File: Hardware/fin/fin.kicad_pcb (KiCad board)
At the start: 2 copper layers, 165.1 x 69.8 mm, 44 parts, among them J1 Conn_01x07, J2 Conn_01x04_Pin, J3 Conn_01x04_Pin, J4 Conn_ARM_SWD_TagConnect_TC203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, J5 Conn_01x04_Pin, U1 ADS131M03QPWRQ1, U2 ADXL380-1BCCZ-RL7, U3 W25N512GVEIG, U4 TMP235A4DBZR, U5 STM32L412K8Ux, U6 ADXL380-1BCCZ-RL7, X1 ECS-327TXO-33-TR

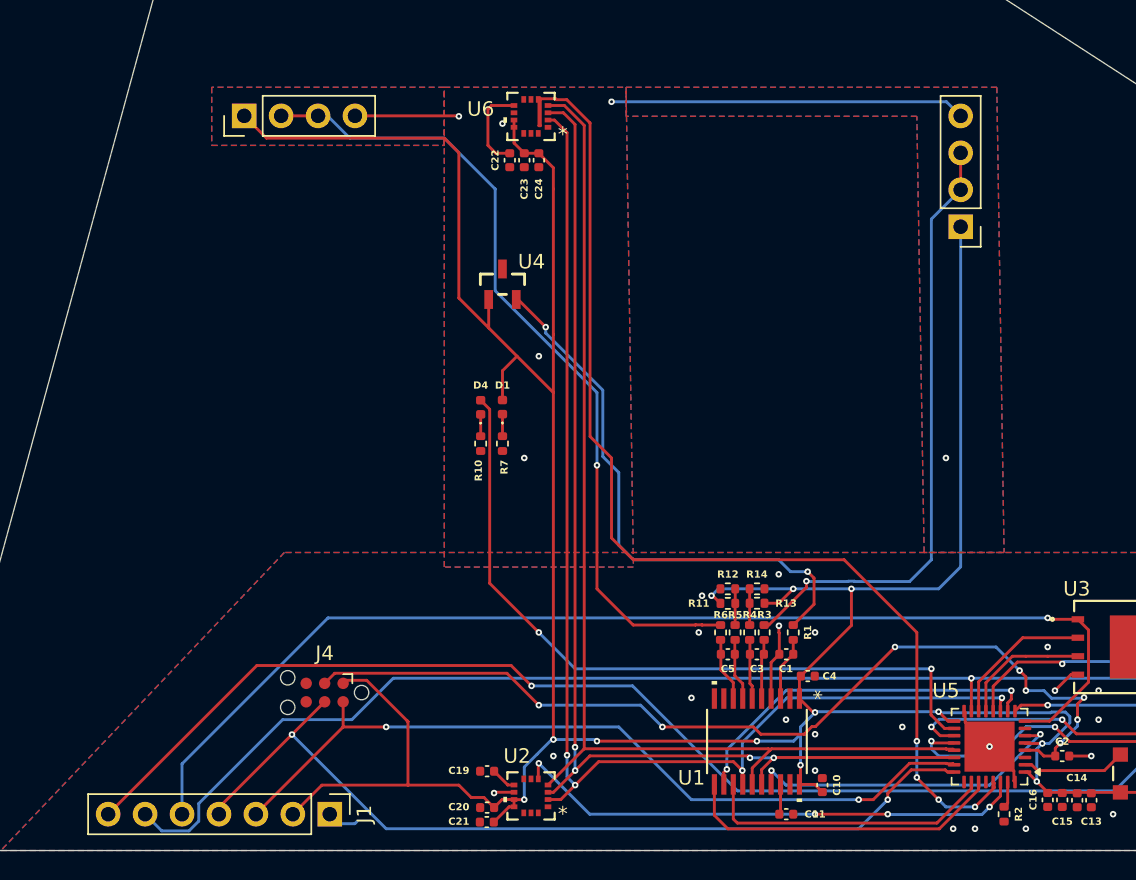
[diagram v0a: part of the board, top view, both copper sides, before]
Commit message: add panel drawing and change connector footprint to use slots
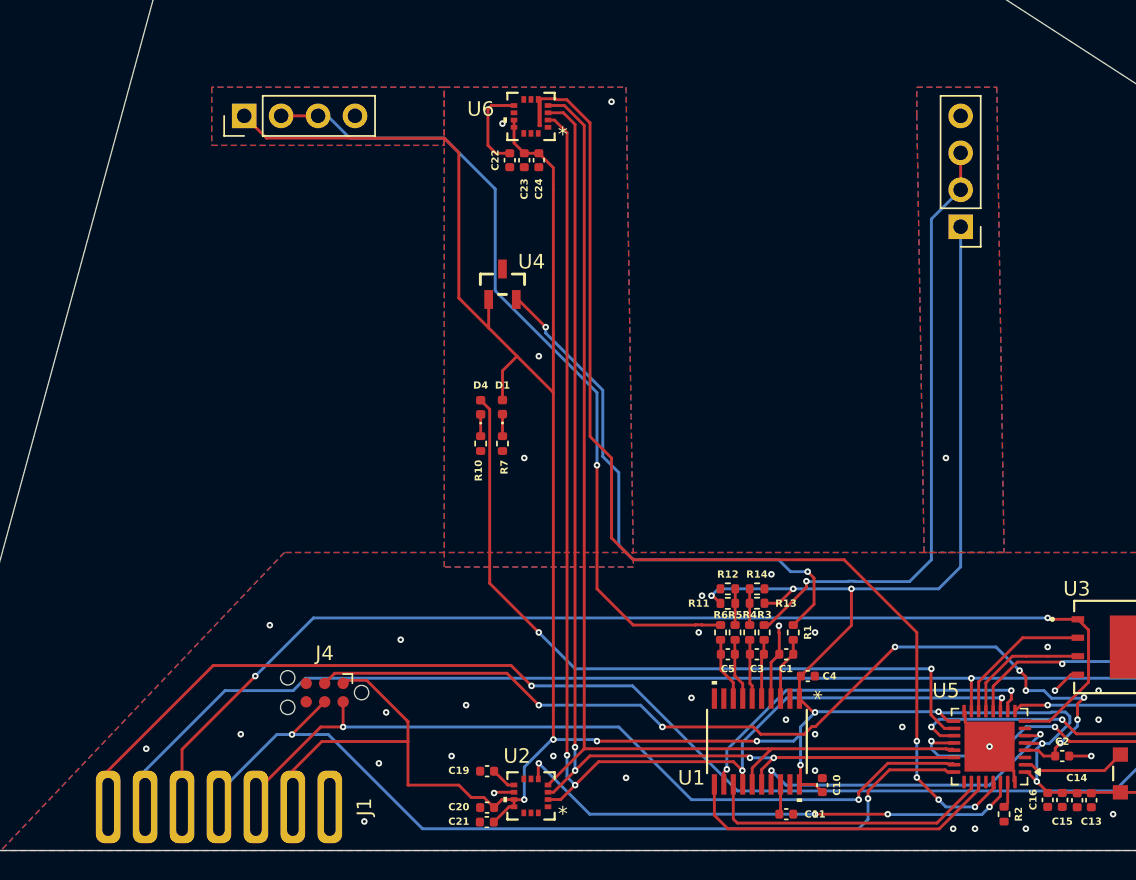
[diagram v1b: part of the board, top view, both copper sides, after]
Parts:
- moved J1 0.50 mm to (98.6, 132.0)
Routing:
- net GND: track 50.3 -> 16.5 mm, vias 30 -> 39
- net +3.3V: track 305.8 -> 308.3 mm
- net SWCLK: track 61.0 -> 62.4 mm
- net QSPI_SCK: track 103.8 -> 105.1 mm
- net SWDIO: track 55.4 -> 56.1 mm
- net ~{FLASH_CS}: track 79.4 -> 79.5 mm, vias 1 -> 2

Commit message: ground pours go brrrrrrrrrrrrrrrrr
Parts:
- J2, J3: footprint Connector_PinHeader_2.54mm:PinHeader_1x04_P2.54mm_Vertical -> Connector_PinHeader_2.54mm:PinHeader_2x02_P2.54mm_Vertical
- moved J3 36.7 mm to (174.0, 110.1), turned to -90 degrees
- moved R10 36.2 mm to (143.5, 118.0), turned to 180 degrees
- moved D4 34.7 mm to (141.0, 118.0), turned to 180 degrees
- moved R7 34.3 mm to (143.5, 116.5), turned to 0 degrees
- moved D1 32.8 mm to (141.0, 116.5), turned to 180 degrees
- moved J2 28.1 mm to (93.1, 112.6)
- moved U4 27.7 mm to (133.5, 111.5), turned to 180 degrees
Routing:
- net STATUS_LED: track 50.8 -> 9.90 mm, vias 2 -> 0
- net +3.3V: track 308.3 -> 281.7 mm, vias 14 -> 17
- net TMP_IN_P: track 38.1 -> 13.6 mm
- net GAUGE1_IN_P: track 56.8 -> 36.3 mm, vias 1 -> 2
- net GAUGE2_IN_P: track 42.5 -> 52.0 mm, vias 1 -> 2
- net QSPI_IO0: track 79.5 -> 81.5 mm
- net GND: vias 39 -> 38

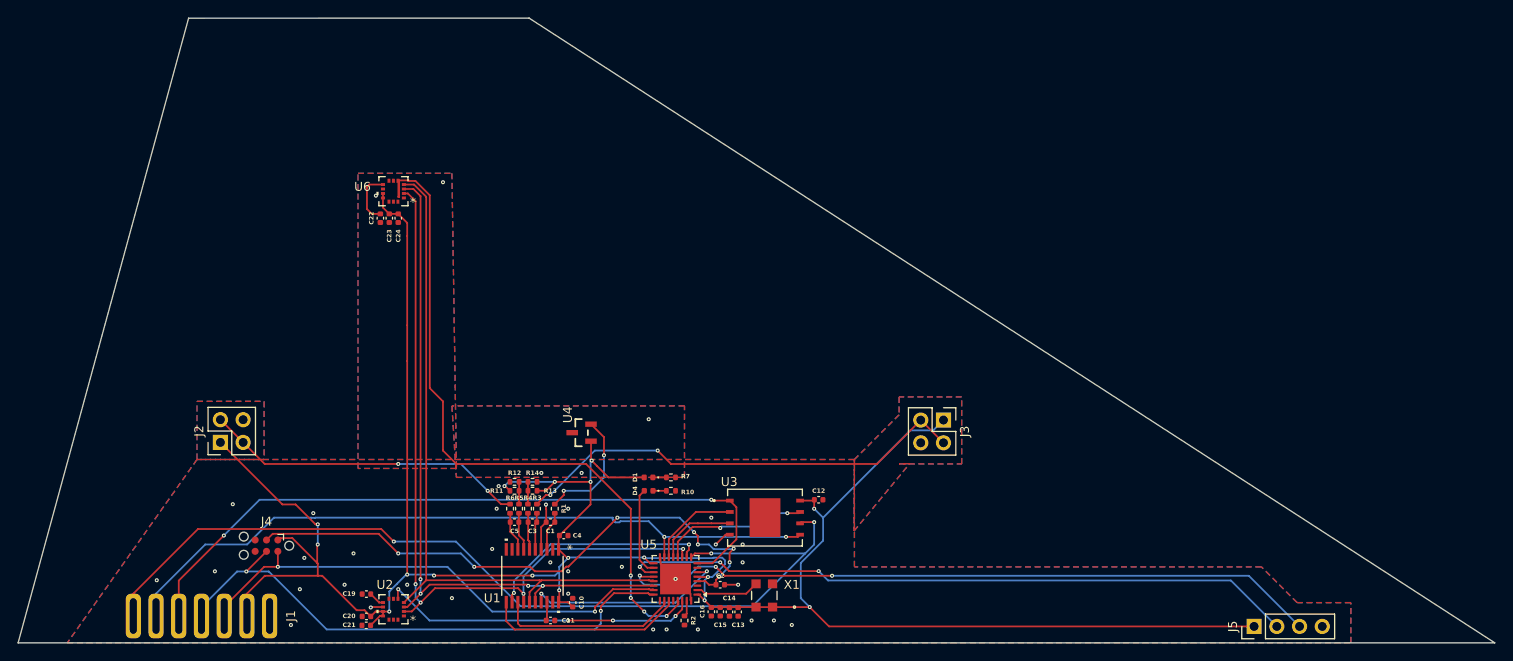
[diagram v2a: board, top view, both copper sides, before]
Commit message: add 1.65V ldo
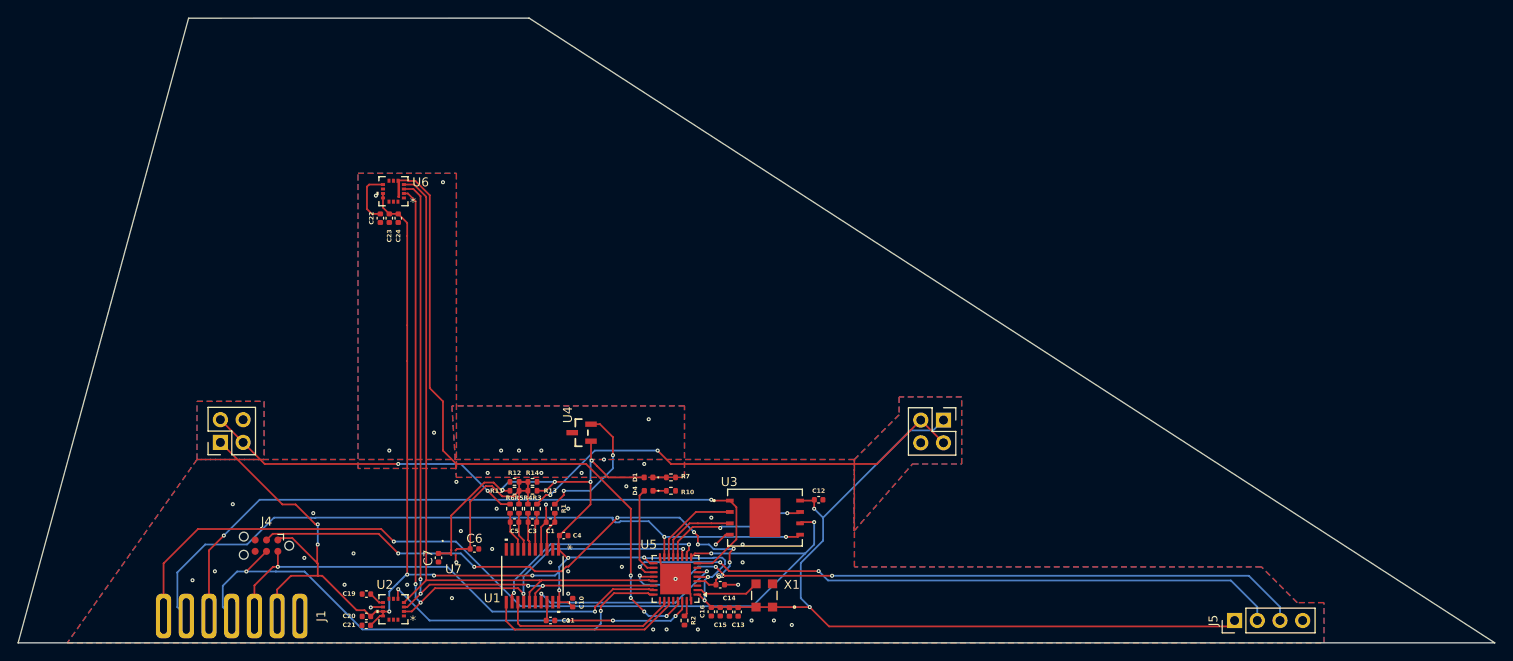
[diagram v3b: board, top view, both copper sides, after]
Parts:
- added C6: 1 uF, Capacitor_SMD:C_0402_1005Metric, F.Cu at (121.5, 124.5)
- added C7: 1 uF, Capacitor_SMD:C_0402_1005Metric, F.Cu at (117.5, 125.5)
- added U7: ADP172ACBZ-1.65-R7, FinLib:CB-4-4_ADI, F.Cu at (119.2, 124.9)
- moved J1 3.38 mm to (102.0, 132.0)
- moved J5 2.28 mm to (206.5, 132.5)
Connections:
- R11 pad 1: GAUGE1_IN_N -> +1.65V
- R12 pad 1: GAUGE1_IN_N -> +1.65V
- R13 pad 2: GAUGE2_IN_N -> +1.65V
- R14 pad 2: GAUGE2_IN_N -> +1.65V
- R4 pad 2: GAUGE2_IN_N -> +1.65V
- R5 pad 1: GAUGE1_IN_N -> +1.65V
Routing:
- net +1.65V: track 0.00 -> 20.9 mm
- net +3.3V: track 281.7 -> 290.7 mm
- net GAUGE1_IN_N: track 2.49 -> 0.00 mm
- net GAUGE2_IN_N: track 2.49 -> 0.00 mm
- net SWDIO: track 56.1 -> 54.1 mm
- net SIGNAL: track 76.2 -> 74.7 mm
- net AVBAY_SYNC: track 79.7 -> 78.2 mm
- net TMP_IN_P: track 13.6 -> 15.0 mm
- net ~{FLASH_CS}: track 79.5 -> 78.1 mm
- net QSPI_SCK: track 105.1 -> 103.7 mm
- net SWCLK: track 62.4 -> 61.4 mm
- net GND: track 16.5 -> 17.4 mm, vias 38 -> 47
- net QSPI_IO0: track 81.5 -> 81.0 mm
